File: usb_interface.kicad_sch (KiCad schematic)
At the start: 55 parts, among them J7 GCT USB4105-GF-A-060, J8 PD_I2C DEBUG, Q1 CSD23280F3, Q2 CSD15380F3, Q3 CSD23280F3, Q4 CSD15380F3, U21 M24512-DFMC6TG, U3 TVS2200DRV, U4 TPD8S300/A, U5 TI TPS25751DREFR

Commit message: organize part fields
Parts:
- C18: Capacitor Rating X5R -> (none); Dielectric (none) -> X7R; MPN (none) -> TCC0402X7R105K250AT; Manufacturer (none) -> CCTC; Tolerance (none) -> 10%
- C184, C19, C24: Capacitor Rating X7R -> (none); Dielectric (none) -> X7R; MPN (none) -> 0402B104J500NT; Manufacturer (none) -> FH (Fenghua); Tolerance (none) -> 5%
- C20, C25, C41, C46: Dielectric (none) -> X7R; MPN (none) -> TCC0402X7R105K250AT; Manufacturer (none) -> CCTC; Tolerance (none) -> 10%; Voltage Rating 16V -> 25V
- C21, C22, C23: Dielectric (none) -> X7R; MPN (none) -> TCC0402X7R103M500AT; Manufacturer (none) -> CCTC; Tolerance (none) -> 20%
- C26, C27, C28, C29, C30, C32, C34: Dielectric (none) -> X7R; MPN (none) -> HGC1206R7106K500NSPJ; Manufacturer (none) -> Chinocera; Tolerance (none) -> 10%
- C31: Dielectric (none) -> X7R; MPN (none) -> HGC0805R7475K500NSLJ; Manufacturer (none) -> Chinocera; Tolerance (none) -> 10%
- C33, C36: Dielectric (none) -> C0G; MPN (none) -> TCC0402COG331F500AT; Manufacturer (none) -> CCTC; Tolerance (none) -> 1%
- C37: Dielectric (none) -> X7R; MPN (none) -> HGC0603R7105K500NTHJ; Manufacturer (none) -> Chinocera; Tolerance (none) -> 10%
- C38, C42, C44: Dielectric (none) -> X5R; MPN (none) -> CGA0805X5R106M500MT; Manufacturer (none) -> HRE; Tolerance (none) -> 20%; Voltage Rating 10V -> 50V
- C39, C43, C45: Dielectric (none) -> X7R; MPN (none) -> TCC0402X7R105K250AT; Manufacturer (none) -> CCTC; Tolerance (none) -> 10%; Voltage Rating 10V -> 25V
- C40: Dielectric (none) -> X5R; MPN (none) -> CGA0805X5R106M500MT; Manufacturer (none) -> HRE; Tolerance (none) -> 20%; Voltage Rating 25V -> 50V
- J7: value GCT USB4105-GF-A-060 -> USB4105-GF-A-060; MPN (none) -> USB4105-GF-A-060; Manufacturer (none) -> GCT
- Q1, Q3: MPN (none) -> CSD23280F3T; Manufacturer (none) -> Texas Instruments
- Q2, Q4: MPN (none) -> CSD15380F3; Manufacturer (none) -> Texas Instruments
- R27: MPN (none) -> ARG02BTC1003; Manufacturer (none) -> Viking Tech; Power Rating (none) -> 62.5mW; Tolerance (none) -> 0.1%
- R28, R30: MPN (none) -> ARG02BTC1003; Manufacturer (none) -> Viking Tech; Power Rating (none) -> 62.5mW; Tolerance 5% -> 0.1%
- R29, R31: MPN (none) -> WF04H1004BTL; Manufacturer (none) -> Walsin; Power Rating (none) -> 100mW; Tolerance 5% -> 0.1%
- R32, R33, R34: MPN (none) -> CRCW04020000Z0EDHP; Manufacturer (none) -> Vishay
- R35, R38: MPN (none) -> FRH0402D1002TS; Manufacturer (none) -> FOJAN; Power Rating (none) -> 62.5mW; Tolerance (none) -> 0.5%
- R36, R37: MPN (none) -> TC0225B2201TCC; Manufacturer (none) -> UNI-ROYAL; Power Rating (none) -> 62.5mW; Tolerance (none) -> 0.1%
- RN1: MPN (none) -> 4D02WGF1002TCE; Manufacturer (none) -> UNI-ROYAL; Power Rating (none) -> 62.5mW; Tolerance (none) -> 1%
- U21: Manufacturer ST(意法半导体) -> STMicroelectronics
- U3: MPN (none) -> TVS2200DRVR; Manufacturer (none) -> Texas Instruments
- U4: value TPD8S300/A -> TPD8S300A; LCSC Part C571205 -> C2649824; Manufacturer TI -> Texas Instruments
- U5: value TI TPS25751DREFR -> TPS25751DREFR; Manufacturer TI(德州仪器) -> Texas Instruments

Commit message: add extra PWR_FLAGs
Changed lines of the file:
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@@
 	)
 	(junction
+		(at 132.08 59.69)
+		(diameter 0)
+		(color 0 0 0 0)
+	)
+	(junction
 		(at 35.56 82.55)
 		(diameter 0)
@@
 	)
 	(junction
+		(at 96.52 67.31)
+		(diameter 0)
+		(color 0 0 0 0)
+	)
+	(junction
 		(at 198.12 109.22)
 		(diameter 0)
@@
 	)
 	(junction
-		(at 93.98 73.66)
+		(at 96.52 73.66)
 		(diameter 0)
 		(color 0 0 0 0)
@@
 	(wire
 		(pts
+			(xy 90.17 67.31) (xy 96.52 67.31)
+		)
+		(stroke
+			(width 0)
+			(type default)
+		)
+	)
+	(wire
+		(pts
 			(xy 179.07 81.28) (xy 186.69 81.28)
 		)
@@
 	(wire
 		(pts
+			(xy 132.08 59.69) (xy 132.08 55.88)
+		)
+		(stroke
+			(width 0)
+			(type default)
+		)
+	)
+	(wire
+		(pts
 			(xy 116.84 158.75) (xy 119.38 158.75)
 		)
@@
 	(wire
 		(pts
+			(xy 90.17 66.04) (xy 90.17 67.31)
+		)
+		(stroke
+			(width 0)
+			(type default)
+		)
+	)
+	(wire
+		(pts
 			(xy 35.56 82.55) (xy 30.48 82.55)
 		)
@@
 	(wire
 		(pts
-			(xy 132.08 62.23) (xy 132.08 55.88)
+			(xy 132.08 62.23) (xy 132.08 59.69)
 		)
 		(stroke
@@
 	(wire
 		(pts
-			(xy 92.71 73.66) (xy 93.98 73.66)
+			(xy 92.71 73.66) (xy 116.84 73.66)
 		)
 		(stroke
@@
 	(wire
 		(pts
-			(xy 93.98 73.66) (xy 116.84 73.66)
-		)
-		(stroke
-			(width 0)
-			(type default)
-		)
-	)
-	(wire
-		(pts
 			(xy 227.33 90.17) (xy 231.14 90.17)
 		)
@@
 	(wire
 		(pts
-			(xy 93.98 72.39) (xy 93.98 73.66)
+			(xy 96.52 60.96) (xy 96.52 67.31)
 		)
 		(stroke
@@
 	(wire
 		(pts
+			(xy 139.7 58.42) (xy 139.7 59.69)
+		)
+		(stroke
+			(width 0)
+			(type default)
+		)
+	)
+	(wire
+		(pts
 			(xy 184.15 109.22) (xy 187.96 109.22)
 		)
@@
 	(wire
 		(pts
+			(xy 96.52 67.31) (xy 96.52 73.66)
+		)
+		(stroke
+			(width 0)
+			(type default)
+		)
+	)
+	(wire
+		(pts
 			(xy 77.47 113.03) (xy 77.47 111.76)
 		)
@@
 	(wire
 		(pts
+			(xy 139.7 59.69) (xy 132.08 59.69)
+		)
+		(stroke
+			(width 0)
+			(type default)
+		)
+	)
+	(wire
+		(pts
 			(xy 63.5 46.99) (xy 86.36 46.99)
 		)
@@
 	)
 	(symbol
+		(lib_id "power:PWR_FLAG")
+		(at 90.17 66.04 0)
+		(unit 1)
+		(body_style 1)
+		(exclude_from_sim no)
+		(in_bom yes)
+		(on_board yes)
+		(in_pos_files yes)
+		(dnp no)
+		(fields_autoplaced yes)
+		(property "Reference" "#FLG011"
+			(at 90.17 64.135 0)
+			(hide yes)
+			(show_name no)
+			(do_not_autoplace no)
+			(effects
+				(font
+					(size 1.27 1.27)
+				)
+			)
+		)
+		(property "Value" "PWR_FLAG"
+			(at 90.17 60.96 0)
+			(show_name no)
+			(do_not_autoplace no)
+			(effects
+				(font
+					(size 1.27 1.27)
+				)
+			)
+		)
+		(property "Footprint" ""
+			(at 90.17 66.04 0)
+			(hide yes)
+			(show_name no)
+			(do_not_autoplace no)
+			(effects
+				(font
+					(size 1.27 1.27)
+				)
+			)
+		)
+		(property "Datasheet" ""
+			(at 90.17 66.04 0)
+			(hide yes)
+			(show_name no)
+			(do_not_autoplace no)
+			(effects
+				(font
+					(size 1.27 1.27)
+				)
+			)
+		)
+		(property "Description" "Special symbol for telling ERC where power comes from"
+			(at 90.17 66.04 0)
+			(hide yes)
+			(show_name no)
+			(do_not_autoplace no)
+			(effects
+				(font
+					(size 1.27 1.27)
+				)
+			)
+		)
+		(pin "1"
+		)
+		(instances
+			(project "parsnip"
+				(path "/a9f1fdad-fb49-4185-a4ff-ad8f47273e4d"
+					(reference "#FLG011")
+					(unit 1)
+				)
+			)
+		)
+	)
+	(symbol
 		(lib_id "Device:R_Small")
 		(at 130.81 148.59 90)
@@
 	)
 	(symbol
+		(lib_id "power:PWR_FLAG")
+		(at 139.7 58.42 0)
+		(unit 1)
+		(body_style 1)
+		(exclude_from_sim no)
+		(in_bom yes)
+		(on_board yes)
+		(in_pos_files yes)
+		(dnp no)
+		(fields_autoplaced yes)
+		(property "Reference" "#FLG012"
+			(at 139.7 56.515 0)
+			(hide yes)
+			(show_name no)
+			(do_not_autoplace no)
+			(effects
+				(font
+					(size 1.27 1.27)
+				)
+			)
+		)
+		(property "Value" "PWR_FLAG"
+			(at 139.7 53.34 0)
+			(show_name no)
+			(do_not_autoplace no)
+			(effects
+				(font
+					(size 1.27 1.27)
+				)
+			)
+		)
+		(property "Footprint" ""
+			(at 139.7 58.42 0)
+			(hide yes)
+			(show_name no)
+			(do_not_autoplace no)
+			(effects
+				(font
+					(size 1.27 1.27)
+				)
+			)
+		)
+		(property "Datasheet" ""
+			(at 139.7 58.42 0)
+			(hide yes)
+			(show_name no)
+			(do_not_autoplace no)
+			(effects
+				(font
+					(size 1.27 1.27)
+				)
+			)
+		)
+		(property "Description" "Special symbol for telling ERC where power comes from"
+			(at 139.7 58.42 0)
+			(hide yes)
+			(show_name no)
+			(do_not_autoplace no)
+			(effects
+				(font
+					(size 1.27 1.27)
+				)
+			)
+		)
+		(pin "1"
+		)
+		(instances
+			(project "parsnip"
+				(path "/a9f1fdad-fb49-4185-a4ff-ad8f47273e4d"
+					(reference "#FLG012")
+					(unit 1)
+				)
+			)
+		)
+	)
+	(symbol
 		(lib_id "Device:R_Small")
 		(at 181.61 60.96 0)
@@
 	(symbol
 		(lib_id "power:VBUS")
-		(at 93.98 72.39 0)
+		(at 96.52 60.96 0)
 		(unit 1)
 		(body_style 1)
@@
 		(fields_autoplaced yes)
 		(property "Reference" "#PWR040"
-			(at 93.98 76.2 0)
+			(at 96.52 64.77 0)
 			(hide yes)
 			(show_name no)
@@
 		)
 		(property "Value" "VBUS"
-			(at 93.98 67.31 0)
+			(at 96.52 55.88 0)
 			(show_name no)
 			(do_not_autoplace no)
@@
 		)
 		(property "Footprint" ""
-			(at 93.98 72.39 0)
+			(at 96.52 60.96 0)
 			(hide yes)
 			(show_name no)
@@
 		)
 		(property "Datasheet" ""
-			(at 93.98 72.39 0)
+			(at 96.52 60.96 0)
 			(hide yes)
 			(show_name no)
@@
 		)
 		(property "Description" "Power symbol creates a global label with name \"VBUS\""
-			(at 93.98 72.39 0)
+			(at 96.52 60.96 0)
 			(hide yes)
 			(show_name no)

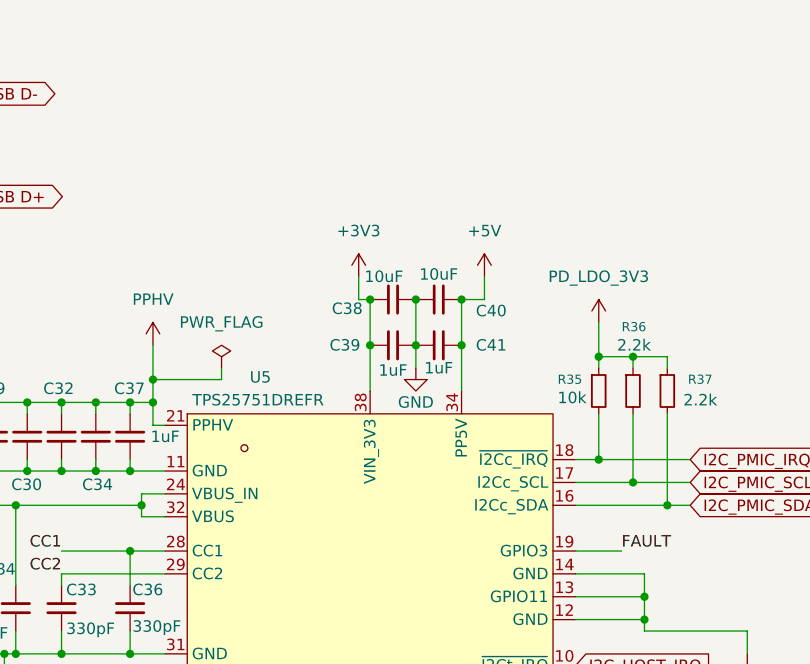
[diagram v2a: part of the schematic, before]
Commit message: routing and silkscreen improvements
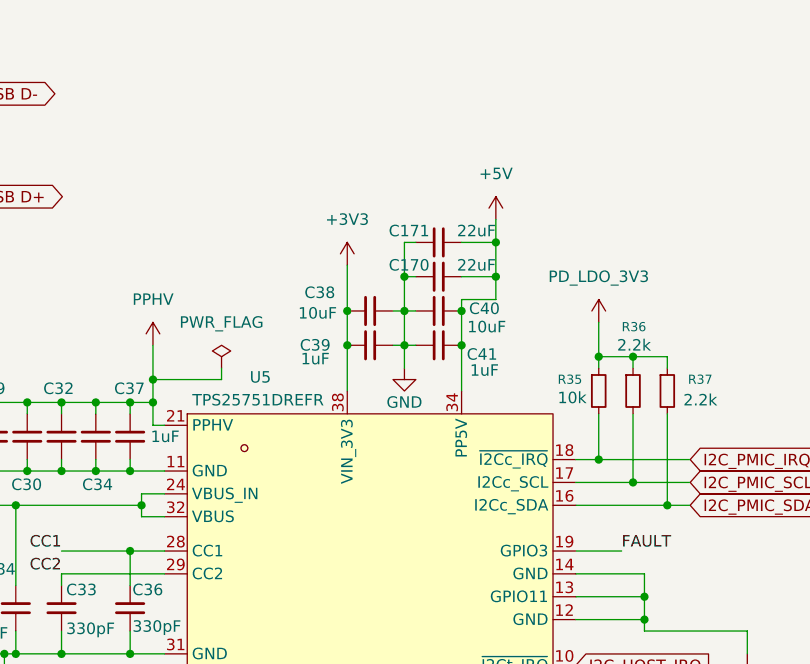
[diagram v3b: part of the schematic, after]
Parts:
- added C170, C171: 22uF, Capacitor_SMD:C_0603_1608Metric, symbol Device:C_Small
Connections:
- net +5V: now also C170.2, C171.2
- net GND: now also C170.1, C171.1
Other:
- moved on the sheet: C38, C39, C40

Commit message: nearly set to order!
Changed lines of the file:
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@@
+	(wire
+		(pts
+			(xy 158.75 52.07) (xy 160.02 52.07)
+		)
+		(stroke
+			(width 0)
+			(type default)
+		)
+	)
 	(wire
 		(pts
@@
 		)
 		(stroke
-			(width 0)
-			(type default)
-		)
-	)
-	(wire
-		(pts
-			(xy 160.02 52.07) (xy 158.75 52.07)
-		)
-		(stroke
